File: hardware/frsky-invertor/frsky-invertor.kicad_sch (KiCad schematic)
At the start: 2 parts, among them Q1 2N7000, Q2 2N7000

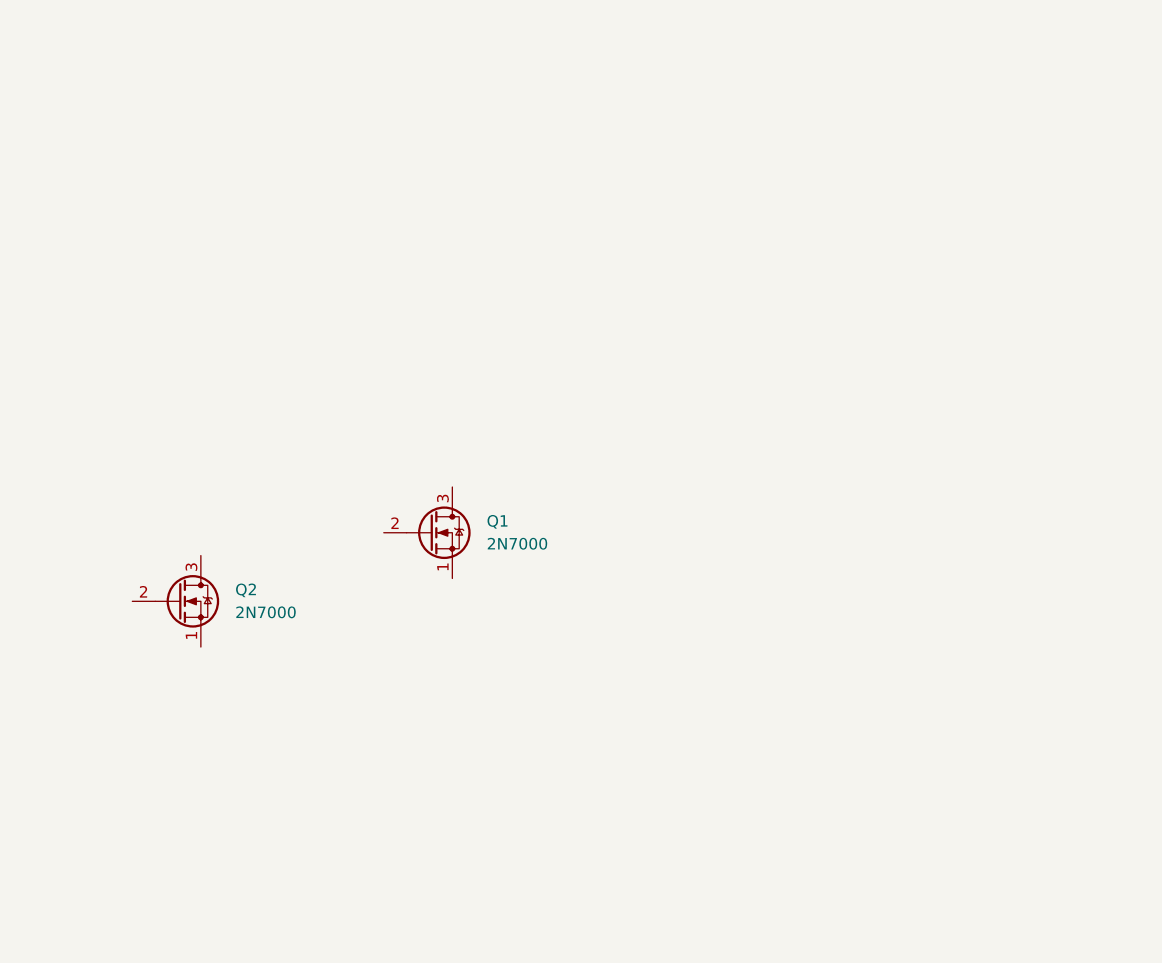
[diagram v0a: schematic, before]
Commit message: Electrical schema created for FrSky invertor.
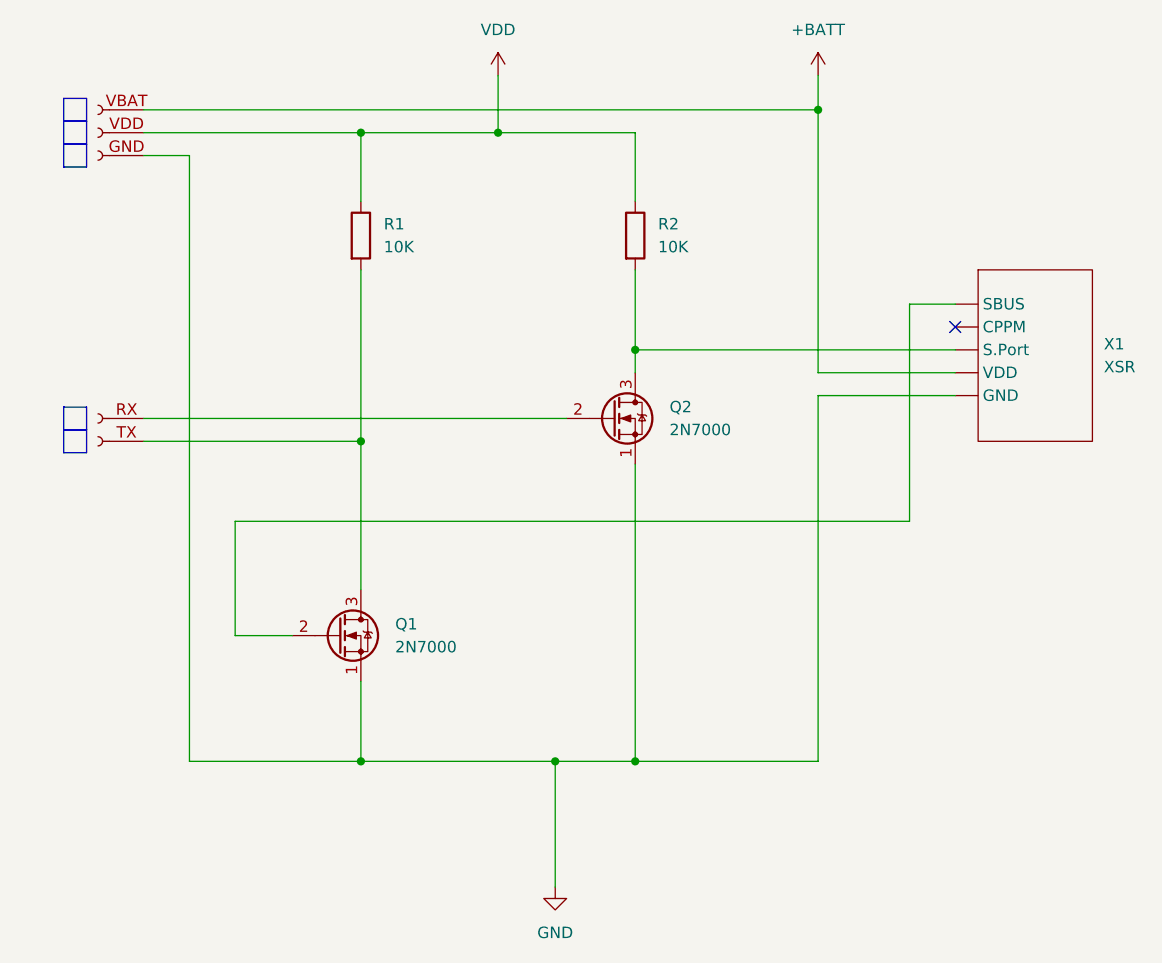
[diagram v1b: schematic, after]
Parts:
- added J1: Conn_01x03_Socket, symbol Connector:Conn_01x03_Socket
- added J2: Conn_01x02_Socket, symbol Connector:Conn_01x02_Socket
- added R1, R2: 10K, symbol Device:R
- added X1: XSR, frsky-invertor:XSR, symbol frsky-invertor:XSR
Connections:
- net GND: now reaches Q1.1 (S)
- net GND: now also Q2.1 (S), J1.GND (3), X1.5 (GND)
- net at Q1.2 (G): now also X1.1 (SBUS)
- net at Q1.3 (D): now also J2.TX (2), R1.2
- net at Q2.2 (G): now also J2.RX (1)
- net at Q2.3 (D): now also R2.2, X1.3 (S.Port)
- new net +BATT: J1.VBAT (1), X1.4 (VDD)
- new net VDD: J1.VDD (2), R1.1, R2.1
- no-connect marks 0 -> 1
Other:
- moved on the sheet: Q1, Q2

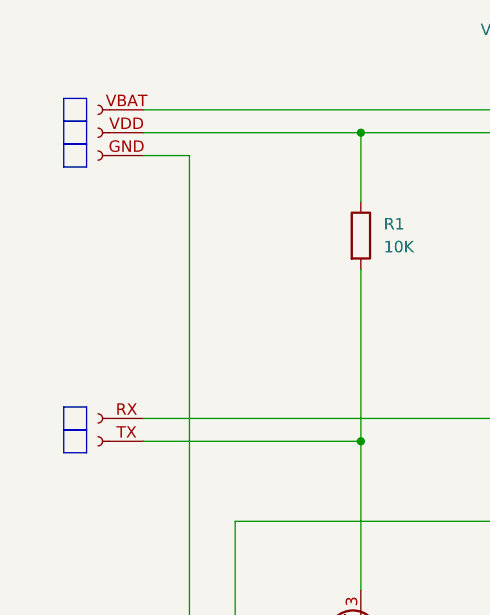
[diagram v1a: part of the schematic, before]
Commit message: Footprints added for resistors and connectors were changed to testpoints.
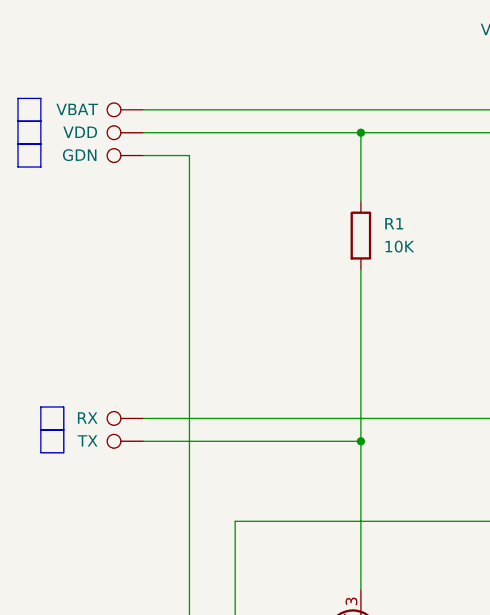
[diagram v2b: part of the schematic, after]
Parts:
- removed J1: Conn_01x03_Socket, symbol Connector:Conn_01x03_Socket
- removed J2: Conn_01x02_Socket, symbol Connector:Conn_01x02_Socket
- added TP1: GDN, Connector_Wire:SolderWire-0.1sqmm_1x01_D0.4mm_OD1mm, symbol Connector:TestPoint
- added TP2: VDD, Connector_Wire:SolderWire-0.1sqmm_1x01_D0.4mm_OD1mm, symbol Connector:TestPoint
- added TP3: VBAT, Connector_Wire:SolderWire-0.1sqmm_1x01_D0.4mm_OD1mm, symbol Connector:TestPoint
- added TP4: TX, Connector_Wire:SolderWire-0.1sqmm_1x01_D0.4mm_OD1mm, symbol Connector:TestPoint
- added TP5: RX, Connector_Wire:SolderWire-0.1sqmm_1x01_D0.4mm_OD1mm, symbol Connector:TestPoint
- Q1, Q2: footprint Package_TO_SOT_THT:TO-92_Inline -> Package_TO_SOT_THT:TO-92_Inline_Wide
- R1, R2: footprint (none) -> Resistor_THT:R_Axial_DIN0414_L11.9mm_D4.5mm_P15.24mm_Horizontal
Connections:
- net +BATT: now also TP3.1
- net GND: now also TP1.1
- net VDD: now also TP2.1
- net at Q1.3 (D), R1.2: now also TP4.1
- net at Q2.2 (G): now also TP5.1
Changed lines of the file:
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@@
+    (stroke (width 0) (type default))
+  )
+  (wire (pts (xy 88.9 44.45) (xy 113.03 44.45))
     (stroke (width 0) (type default))
   )
@@
     (stroke (width 0) (type default))
   )
-  (wire (pts (xy 88.9 44.45) (xy 113.03 44.45))
-    (stroke (width 0) (type default))
-  )
   (wire (pts (xy 128.27 44.45) (xy 143.51 44.45))
     (stroke (width 0) (type default))
@@
     (stroke (width 0) (type default))
   )
-  (rectangle (start 80.01 40.64) (end 82.55 43.18)
+  (rectangle (start 74.93 40.64) (end 77.47 43.18)
     (stroke (width 0) (type default) (color 0 0 0 1))
     (fill (type color) (color 255 127 39 1))
   )
-  (rectangle (start 80.01 74.93) (end 82.55 77.47)
+  (rectangle (start 77.47 74.93) (end 80.01 77.47)
     (stroke (width 0) (type default) (color 0 0 0 1))
     (fill (type color) (color 34 177 76 1))
   )
-  (rectangle (start 80.01 43.18) (end 82.55 45.72)
+  (rectangle (start 74.93 43.18) (end 77.47 45.72)
     (stroke (width 0) (type default) (color 0 0 0 1))
     (fill (type color) (color 255 0 0 1))
   )
-  (rectangle (start 80.01 45.72) (end 82.55 48.26)
+  (rectangle (start 74.93 45.72) (end 77.47 48.26)
     (stroke (width 0) (type default) (color 0 0 0 1))
     (fill (type color) (color 0 0 0 1))
   )
-  (rectangle (start 80.01 77.47) (end 82.55 80.01)
+  (rectangle (start 77.47 77.47) (end 80.01 80.01)
     (stroke (width 0) (type default) (color 0 0 0 1))
     (fill (type color) (color 255 242 0 1))
   )
-  (symbol (lib_id "Connector:Conn_01x03_Socket") (at 83.82 44.45 0) (mirror y) (unit 1)
-    (in_bom yes) (on_board yes) (dnp no)
-    (property "Reference" "J1" (at 82.55 43.18 0)
-      (effects (font (size 1.27 1.27)) (justify left) hide)
-    )
-    (property "Value" "Conn_01x03_Socket" (at 82.55 45.72 0)
-      (effects (font (size 1.27 1.27)) (justify left) hide)
-    )
-    (property "Footprint" "" (at 83.82 44.45 0)
-      (effects (font (size 1.27 1.27)) hide)
-    )
-    (property "Datasheet" "~" (at 83.82 44.45 0)
-      (effects (font (size 1.27 1.27)) hide)
-    )
-    (pin "VDD")
-    (pin "VBAT")
-    (pin "GND")
-    (instances
-      (project "frsky-invertor"
-        (path "/61f24ab4-e0f3-4c10-8a17-5d7bc94342fe"
-          (reference "J1") (unit 1)
-        )
-      )
-    )
-  )
   (symbol (lib_id "Device:R") (at 143.51 55.88 0) (unit 1)
     (in_bom yes) (on_board yes) (dnp no)
@@
       (effects (font (size 1.27 1.27)) (justify left))
     )
-    (property "Footprint" "" (at 141.732 55.88 90)
+    (property "Footprint" "Resistor_THT:R_Axial_DIN0414_L11.9mm_D4.5mm_P15.24mm_Horizontal" (at 141.732 55.88 90)
       (effects (font (size 1.27 1.27)) hide)
     )
@@
       (effects (font (size 1.27 1.27)) (justify left))
     )
-    (property "Footprint" "" (at 111.252 55.88 90)
+    (property "Footprint" "Resistor_THT:R_Axial_DIN0414_L11.9mm_D4.5mm_P15.24mm_Horizontal" (at 111.252 55.88 90)
       (effects (font (size 1.27 1.27)) hide)
     )
@@
       (effects (font (size 1.27 1.27)) (justify left))
     )
-    (property "Footprint" "Package_TO_SOT_THT:TO-92_Inline" (at 115.57 102.235 0)
+    (property "Footprint" "Package_TO_SOT_THT:TO-92_Inline_Wide" (at 115.57 102.235 0)
       (effects (font (size 1.27 1.27) italic) (justify left) hide)
     )
@@
     )
   )
+  (symbol (lib_id "Connector:TestPoint") (at 88.9 46.99 90) (unit 1)
+    (in_bom yes) (on_board yes) (dnp no)
+    (property "Reference" "TP1" (at 85.598 41.91 90)
+      (effects (font (size 1.27 1.27)) hide)
+    )
+    (property "Value" "GDN" (at 83.82 46.99 90)
+      (effects (font (size 1.27 1.27)) (justify left))
+    )
+    (property "Footprint" "Connector_Wire:SolderWire-0.1sqmm_1x01_D0.4mm_OD1mm" (at 88.9 41.91 0)
+      (effects (font (size 1.27 1.27)) hide)
+    )
+    (property "Datasheet" "~" (at 88.9 41.91 0)
+      (effects (font (size 1.27 1.27)) hide)
+    )
+    (pin "1")
+    (instances
+      (project "frsky-invertor"
+        (path "/61f24ab4-e0f3-4c10-8a17-5d7bc94342fe"
+          (reference "TP1") (unit 1)
+        )
+      )
+    )
+  )
   (symbol (lib_id "power:GND") (at 134.62 128.27 0) (unit 1)
     (in_bom yes) (on_board yes) (dnp no) (fields_autoplaced)
@@
       (effects (font (size 1.27 1.27)) (justify left))
     )
-    (property "Footprint" "Package_TO_SOT_THT:TO-92_Inline" (at 146.05 78.105 0)
+    (property "Footprint" "Package_TO_SOT_THT:TO-92_Inline_Wide" (at 146.05 78.105 0)
       (effects (font (size 1.27 1.27) italic) (justify left) hide)
     )
@@
     )
   )
+  (symbol (lib_id "Connector:TestPoint") (at 88.9 44.45 90) (unit 1)
+    (in_bom yes) (on_board yes) (dnp no)
+    (property "Reference" "TP2" (at 85.598 39.37 90)
+      (effects (font (size 1.27 1.27)) hide)
+    )
+    (property "Value" "VDD" (at 83.82 44.45 90)
+      (effects (font (size 1.27 1.27)) (justify left))
+    )
+    (property "Footprint" "Connector_Wire:SolderWire-0.1sqmm_1x01_D0.4mm_OD1mm" (at 88.9 39.37 0)
+      (effects (font (size 1.27 1.27)) hide)
+    )
+    (property "Datasheet" "~" (at 88.9 39.37 0)
+      (effects (font (size 1.27 1.27)) hide)
+    )
+    (pin "1")
+    (instances
+      (project "frsky-invertor"
+        (path "/61f24ab4-e0f3-4c10-8a17-5d7bc94342fe"
+          (reference "TP2") (unit 1)
+        )
+      )
+    )
+  )
   (symbol (lib_id "power:VDD") (at 128.27 38.1 0) (unit 1)
     (in_bom yes) (on_board yes) (dnp no) (fields_autoplaced)
@@
         (path "/61f24ab4-e0f3-4c10-8a17-5d7bc94342fe"
           (reference "#PWR02") (unit 1)
+        )
+      )
+    )
+  )
+  (symbol (lib_id "Connector:TestPoint") (at 88.9 78.74 90) (unit 1)
+    (in_bom yes) (on_board yes) (dnp no)
+    (property "Reference" "TP4" (at 85.598 73.66 90)
+      (effects (font (size 1.27 1.27)) hide)
+    )
+    (property "Value" "TX" (at 83.82 78.74 90)
+      (effects (font (size 1.27 1.27)) (justify left))
+    )
+    (property "Footprint" "Connector_Wire:SolderWire-0.1sqmm_1x01_D0.4mm_OD1mm" (at 88.9 73.66 0)
+      (effects (font (size 1.27 1.27)) hide)
+    )
+    (property "Datasheet" "~" (at 88.9 73.66 0)
+      (effects (font (size 1.27 1.27)) hide)
+    )
+    (pin "1")
+    (instances
+      (project "frsky-invertor"
+        (path "/61f24ab4-e0f3-4c10-8a17-5d7bc94342fe"
+          (reference "TP4") (unit 1)
         )
       )
@@
     )
   )
-  (symbol (lib_id "Connector:Conn_01x02_Socket") (at 83.82 76.2 0) (mirror y) (unit 1)
-    (in_bom yes) (on_board yes) (dnp no)
-    (property "Reference" "J2" (at 82.55 76.2 0)
-      (effects (font (size 1.27 1.27)) (justify left) hide)
-    )
-    (property "Value" "Conn_01x02_Socket" (at 82.55 78.74 0)
-      (effects (font (size 1.27 1.27)) (justify left) hide)
-    )
-    (property "Footprint" "" (at 83.82 76.2 0)
-      (effects (font (size 1.27 1.27)) hide)
-    )
-    (property "Datasheet" "~" (at 83.82 76.2 0)
-      (effects (font (size 1.27 1.27)) hide)
-    )
-    (pin "TX")
-    (pin "RX")
-    (instances
-      (project "frsky-invertor"
-        (path "/61f24ab4-e0f3-4c10-8a17-5d7bc94342fe"
-          (reference "J2") (unit 1)
-        )
-      )
+  (symbol (lib_id "Connector:TestPoint") (at 88.9 41.91 90) (unit 1)
+    (in_bom yes) (on_board yes) (dnp no)
+    (property "Reference" "TP3" (at 85.598 36.83 90)
+      (effects (font (size 1.27 1.27)) hide)
+    )
+    (property "Value" "VBAT" (at 83.82 41.91 90)
+      (effects (font (size 1.27 1.27)) (justify left))
+    )
+    (property "Footprint" "Connector_Wire:SolderWire-0.1sqmm_1x01_D0.4mm_OD1mm" (at 88.9 36.83 0)
+      (effects (font (size 1.27 1.27)) hide)
+    )
+    (property "Datasheet" "~" (at 88.9 36.83 0)
+      (effects (font (size 1.27 1.27)) hide)
+    )
+    (pin "1")
+    (instances
+      (project "frsky-invertor"
+        (path "/61f24ab4-e0f3-4c10-8a17-5d7bc94342fe"
+          (reference "TP3") (unit 1)
+        )
+      )
+    )
+  )
+  (symbol (lib_id "Connector:TestPoint") (at 88.9 76.2 90) (unit 1)
+    (in_bom yes) (on_board yes) (dnp no)
+    (property "Reference" "TP5" (at 85.598 71.12 90)
+      (effects (font (size 1.27 1.27)) hide)
+    )
+    (property "Value" "RX" (at 83.82 76.2 90)
+      (effects (font (size 1.27 1.27)) (justify left))
+    )
+    (property "Footprint" "Connector_Wire:SolderWire-0.1sqmm_1x01_D0.4mm_OD1mm" (at 88.9 71.12 0)
+      (effects (font (size 1.27 1.27)) hide)
+    )
+    (property "Datasheet" "~" (at 88.9 71.12 0)
+      (effects (font (size 1.27 1.27)) hide)
+    )
+    (pin "1")
+    (instances
+      (project "frsky-invertor"
+        (path "/61f24ab4-e0f3-4c10-8a17-5d7bc94342fe"
+          (reference "TP5") (unit 1)
+        )
+      )

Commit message: PCB layout created.
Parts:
- R1, R2: footprint Resistor_THT:R_Axial_DIN0414_L11.9mm_D4.5mm_P15.24mm_Horizontal -> Resistor_THT:R_Axial_DIN0411_L9.9mm_D3.6mm_P12.70mm_Horizontal
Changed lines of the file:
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@@
       (effects (font (size 1.27 1.27)) (justify left))
     )
-    (property "Footprint" "Resistor_THT:R_Axial_DIN0414_L11.9mm_D4.5mm_P15.24mm_Horizontal" (at 141.732 55.88 90)
+    (property "Footprint" "Resistor_THT:R_Axial_DIN0411_L9.9mm_D3.6mm_P12.70mm_Horizontal" (at 141.732 55.88 90)
       (effects (font (size 1.27 1.27)) hide)
     )
@@
       (effects (font (size 1.27 1.27)) (justify left))
     )
-    (property "Footprint" "Resistor_THT:R_Axial_DIN0414_L11.9mm_D4.5mm_P15.24mm_Horizontal" (at 111.252 55.88 90)
+    (property "Footprint" "Resistor_THT:R_Axial_DIN0411_L9.9mm_D3.6mm_P12.70mm_Horizontal" (at 111.252 55.88 90)
       (effects (font (size 1.27 1.27)) hide)
     )
